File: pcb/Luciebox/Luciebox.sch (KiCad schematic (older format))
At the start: 60 parts, among them J1 Screw_Terminal_01x07, J2 Screw_Terminal_01x07, J3 Screw_Terminal_01x07, J4 Screw_Terminal_01x07, J5 Screw_Terminal_01x07, J7 USB_B_Mini, P1 CONN_01X01, P2 CONN_01X01, P3 CONN_01X01, P4 CONN_01X01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

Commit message: progressive change towards v2.0
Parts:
- removed J1: Screw_Terminal_01x07, Luciebox:Terminal_7x1_100mil, symbol Luciebox_components:Screw_Terminal_01x07_mirror
- added T? (x2): terminal_8x1, Luciebox:Terminal_8x1_100mil, symbol Luciebox_components:terminal_8x1
- R1, R10, R11, R12, R13, R14, R15, R16, R17, R18, R19, R2, R3, R4, R47, R48, R49, R5, R6, R7, R8, R9: footprint Luciebox:1206 -> Luciebox:1206_0805
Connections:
- net 0(Rx): now also T?.8
- net 12(MISO): now also T?.5
- net 13(SCK): now also T?.6
- net 2: now also T?.2
- net 3(PWM): now also T?.7
- net 4: now also T?.3
- net 7: now also T?.1
- net 8: now also T?.4
- net VCC: now also T?.1, T?.2, T?.3, T?.4, T?.5, T?.6, T?.7, T?.8
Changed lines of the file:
@@
 F 0 "R3" H 7059 2446 50  0000 L CNN
 F 1 "100" H 7059 2355 50  0000 L CNN
-F 2 "Luciebox:1206" H 7000 2400 50  0001 C CNN
+F 2 "Luciebox:1206_0805" H 7000 2400 50  0001 C CNN
 F 3 "~" H 7000 2400 50  0001 C CNN
 	1    7000 2400
@@
 F 0 "R4" H 7309 2446 50  0000 L CNN
 F 1 "100" H 7309 2355 50  0000 L CNN
-F 2 "Luciebox:1206" H 7250 2400 50  0001 C CNN
+F 2 "Luciebox:1206_0805" H 7250 2400 50  0001 C CNN
 F 3 "~" H 7250 2400 50  0001 C CNN
 	1    7250 2400
@@
 F 0 "R5" H 7559 2446 50  0000 L CNN
 F 1 "100" H 7559 2355 50  0000 L CNN
-F 2 "Luciebox:1206" H 7500 2400 50  0001 C CNN
+F 2 "Luciebox:1206_0805" H 7500 2400 50  0001 C CNN
 F 3 "~" H 7500 2400 50  0001 C CNN
 	1    7500 2400
@@
 	3350 1600 3500 1600
 Wire Wire Line
-	3350 1700 3850 1700
-Wire Wire Line
 	3700 2500 3700 1200
 Connection ~ 3700 1200
@@
 F 0 "R2" H 6809 2446 50  0000 L CNN
 F 1 "100" H 6809 2355 50  0000 L CNN
-F 2 "Luciebox:1206" H 6750 2400 50  0001 C CNN
+F 2 "Luciebox:1206_0805" H 6750 2400 50  0001 C CNN
 F 3 "~" H 6750 2400 50  0001 C CNN
 	1    6750 2400
@@
 F 0 "R1" H 6559 2446 50  0000 L CNN
 F 1 "100" H 6559 2355 50  0000 L CNN
-F 2 "Luciebox:1206" H 6500 2400 50  0001 C CNN
+F 2 "Luciebox:1206_0805" H 6500 2400 50  0001 C CNN
 F 3 "~" H 6500 2400 50  0001 C CNN
 	1    6500 2400
@@
 F 3 "~" H 5450 2600 50  0001 C CNN
 	1    5450 2600
-	1    0    0    -1
-$EndComp
-$Comp
-L Luciebox_components:Screw_Terminal_01x07_mirror J1
-U 1 1 5D554824
-P 3200 2600
-F 0 "J1" H 3282 3117 50  0000 C CNN
-F 1 "Screw_Terminal_01x07" H 3282 3026 50  0000 C CNN
-F 2 "Luciebox:Terminal_7x1_100mil" H 3200 2600 50  0001 C CNN
-F 3 "~" H 3200 2600 50  0001 C CNN
-	1    3200 2600
 	1    0    0    -1
 $EndComp
@@
 F 0 "R7" H 1009 4946 50  0000 L CNN
 F 1 "10K" H 1009 4855 50  0000 L CNN
-F 2 "Luciebox:1206" H 950 4900 50  0001 C CNN
+F 2 "Luciebox:1206_0805" H 950 4900 50  0001 C CNN
 F 3 "~" H 950 4900 50  0001 C CNN
 	1    950  4900
@@
 F 0 "R8" H 1309 4946 50  0000 L CNN
 F 1 "10K" H 1309 4855 50  0000 L CNN
-F 2 "Luciebox:1206" H 1250 4900 50  0001 C CNN
+F 2 "Luciebox:1206_0805" H 1250 4900 50  0001 C CNN
 F 3 "~" H 1250 4900 50  0001 C CNN
 	1    1250 4900
@@
 F 0 "R9" H 1609 4946 50  0000 L CNN
 F 1 "10K" H 1609 4855 50  0000 L CNN
-F 2 "Luciebox:1206" H 1550 4900 50  0001 C CNN
+F 2 "Luciebox:1206_0805" H 1550 4900 50  0001 C CNN
 F 3 "~" H 1550 4900 50  0001 C CNN
 	1    1550 4900
@@
 F 0 "R10" H 1909 4946 50  0000 L CNN
 F 1 "10K" H 1909 4855 50  0000 L CNN
-F 2 "Luciebox:1206" H 1850 4900 50  0001 C CNN
+F 2 "Luciebox:1206_0805" H 1850 4900 50  0001 C CNN
 F 3 "~" H 1850 4900 50  0001 C CNN
 	1    1850 4900
@@
 F 0 "R11" H 2209 4946 50  0000 L CNN
 F 1 "10K" H 2209 4855 50  0000 L CNN
-F 2 "Luciebox:1206" H 2150 4900 50  0001 C CNN
+F 2 "Luciebox:1206_0805" H 2150 4900 50  0001 C CNN
 F 3 "~" H 2150 4900 50  0001 C CNN
 	1    2150 4900
@@
 F 0 "R12" H 2509 4946 50  0000 L CNN
 F 1 "10K" H 2509 4855 50  0000 L CNN
-F 2 "Luciebox:1206" H 2450 4900 50  0001 C CNN
+F 2 "Luciebox:1206_0805" H 2450 4900 50  0001 C CNN
 F 3 "~" H 2450 4900 50  0001 C CNN
 	1    2450 4900
@@
 F 0 "R13" H 2809 4946 50  0000 L CNN
 F 1 "10K" H 2809 4855 50  0000 L CNN
-F 2 "Luciebox:1206" H 2750 4900 50  0001 C CNN
+F 2 "Luciebox:1206_0805" H 2750 4900 50  0001 C CNN
 F 3 "~" H 2750 4900 50  0001 C CNN
 	1    2750 4900
@@
 F 0 "R14" H 3109 4946 50  0000 L CNN
 F 1 "10K" H 3109 4855 50  0000 L CNN
-F 2 "Luciebox:1206" H 3050 4900 50  0001 C CNN
+F 2 "Luciebox:1206_0805" H 3050 4900 50  0001 C CNN
 F 3 "~" H 3050 4900 50  0001 C CNN
 	1    3050 4900
@@
 F 0 "R15" H 3409 4946 50  0000 L CNN
 F 1 "10K" H 3409 4855 50  0000 L CNN
-F 2 "Luciebox:1206" H 3350 4900 50  0001 C CNN
+F 2 "Luciebox:1206_0805" H 3350 4900 50  0001 C CNN
 F 3 "~" H 3350 4900 50  0001 C CNN
 	1    3350 4900
@@
 F 0 "R16" H 3709 4946 50  0000 L CNN
 F 1 "10K" H 3709 4855 50  0000 L CNN
-F 2 "Luciebox:1206" H 3650 4900 50  0001 C CNN
+F 2 "Luciebox:1206_0805" H 3650 4900 50  0001 C CNN
 F 3 "~" H 3650 4900 50  0001 C CNN
 	1    3650 4900
@@
 F 0 "R17" H 4009 4946 50  0000 L CNN
 F 1 "10K" H 4009 4855 50  0000 L CNN
-F 2 "Luciebox:1206" H 3950 4900 50  0001 C CNN
+F 2 "Luciebox:1206_0805" H 3950 4900 50  0001 C CNN
 F 3 "~" H 3950 4900 50  0001 C CNN
 	1    3950 4900
@@
 F 0 "R18" H 4309 4946 50  0000 L CNN
 F 1 "10K" H 4309 4855 50  0000 L CNN
-F 2 "Luciebox:1206" H 4250 4900 50  0001 C CNN
+F 2 "Luciebox:1206_0805" H 4250 4900 50  0001 C CNN
 F 3 "~" H 4250 4900 50  0001 C CNN
 	1    4250 4900
@@
 F 0 "R6" H 9359 4496 50  0000 L CNN
 F 1 "1M" H 9359 4405 50  0000 L CNN
-F 2 "Luciebox:1206" H 9300 4450 50  0001 C CNN
+F 2 "Luciebox:1206_0805" H 9300 4450 50  0001 C CNN
 F 3 "~" H 9300 4450 50  0001 C CNN
 	1    9300 4450
@@
 F 0 "R19" H 9559 5296 50  0000 L CNN
 F 1 "100" H 9559 5205 50  0000 L CNN
-F 2 "Luciebox:1206" H 9500 5250 50  0001 C CNN
+F 2 "Luciebox:1206_0805" H 9500 5250 50  0001 C CNN
 F 3 "~" H 9500 5250 50  0001 C CNN
 	1    9500 5250
@@
 F 0 "R47" H 3409 6646 50  0000 L CNN
 F 1 "100K" H 3409 6555 50  0000 L CNN
-F 2 "Luciebox:1206" H 3350 6600 50  0001 C CNN
+F 2 "Luciebox:1206_0805" H 3350 6600 50  0001 C CNN
 F 3 "~" H 3350 6600 50  0001 C CNN
 	1    3350 6600
@@
 F 0 "R48" H 3409 7046 50  0000 L CNN
 F 1 "100K" H 3409 6955 50  0000 L CNN
-F 2 "Luciebox:1206" H 3350 7000 50  0001 C CNN
+F 2 "Luciebox:1206_0805" H 3350 7000 50  0001 C CNN
 F 3 "~" H 3350 7000 50  0001 C CNN
 	1    3350 7000
@@
 F 0 "R49" H 3109 3546 50  0000 L CNN
 F 1 "10K" H 3109 3455 50  0000 L CNN
-F 2 "Luciebox:1206" H 3050 3500 50  0001 C CNN
+F 2 "Luciebox:1206_0805" H 3050 3500 50  0001 C CNN
 F 3 "~" H 3050 3500 50  0001 C CNN
 	1    3050 3500
@@
 Wire Wire Line
 	4150 5600 4050 5600
+$Comp
+L power:VCC #PWR?
+U 1 1 5E92F10F
+P 2250 2350
+F 0 "#PWR?" H 2250 2200 50  0001 C CNN
+F 1 "VCC" H 2267 2523 50  0000 C CNN
+F 2 "" H 2250 2350 50  0001 C CNN
+F 3 "" H 2250 2350 50  0001 C CNN
+	1    2250 2350
+	1    0    0    -1
+$EndComp
+$Comp
+L Luciebox_components:terminal_8x1 T?
+U 1 1 5E94AD11
+P 3350 2300
+F 0 "T?" H 3467 2085 50  0000 C CNN
+F 1 "terminal_8x1" H 3467 2176 50  0000 C CNN
+F 2 "Luciebox:Terminal_8x1_100mil" H 3150 2200 50  0001 C CNN
+F 3 "" H 3300 3400 50  0001 C CNN
+	1    3350 2300
+	-1   0    0    1
+$EndComp
+$Comp
+L Luciebox_components:terminal_8x1 T?
+U 1 1 5E968FAE
+P 2600 2300
+F 0 "T?" H 2717 2085 50  0000 C CNN
+F 1 "terminal_8x1" H 2717 2176 50  0000 C CNN
+F 2 "Luciebox:Terminal_8x1_100mil" H 2400 2200 50  0001 C CNN
+F 3 "" H 2550 3400 50  0001 C CNN
+	1    2600 2300
+	1    0    0    1
+$EndComp
+Wire Wire Line
+	2550 2300 2300 2300
+Wire Wire Line
+	2300 2300 2300 2350
+Wire Wire Line
+	2300 2350 2250 2350
+Wire Wire Line
+	2550 2400 2300 2400
+Wire Wire Line
+	2300 2400 2300 2350
+Connection ~ 2300 2350
+Wire Wire Line
+	2550 2500 2300 2500
+Wire Wire Line
+	2300 2500 2300 2400
+Connection ~ 2300 2400
+Wire Wire Line
+	2300 2500 2300 2600
+Wire Wire Line
+	2300 2600 2550 2600
+Connection ~ 2300 2500
+Wire Wire Line
+	2550 2700 2300 2700
+Wire Wire Line
+	2300 2700 2300 2600
+Connection ~ 2300 2600
+Wire Wire Line
+	2550 2800 2300 2800
+Wire Wire Line
+	2300 2800 2300 2700
+Connection ~ 2300 2700
+Wire Wire Line
+	2550 2900 2300 2900
+Wire Wire Line
+	2300 2900 2300 2800
+Connection ~ 2300 2800
+Wire Wire Line
+	2550 3000 2300 3000
+Wire Wire Line
+	2300 3000 2300 2900
+Connection ~ 2300 2900
+Wire Wire Line
+	3350 1700 3450 1700
+Wire Wire Line
+	3400 3000 3450 3000
+Wire Wire Line
+	3450 3000 3450 1700
+Connection ~ 3450 1700
+Wire Wire Line
+	3450 1700 3850 1700
 $EndSCHEMATC

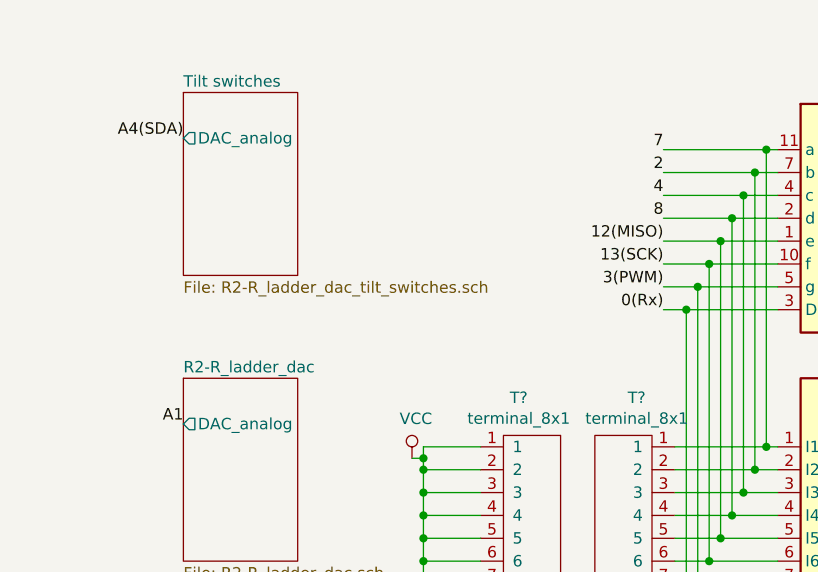
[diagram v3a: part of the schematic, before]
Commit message: add holes for R-2R ladder, fix bug with tilt switch sheet. Set output led's. All good here.
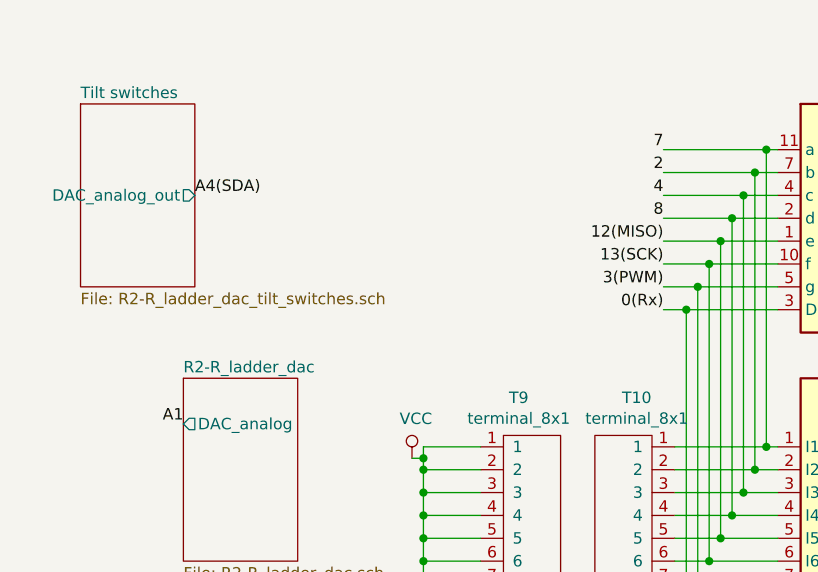
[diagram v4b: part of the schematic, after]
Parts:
- gave numbers to parts that had none: 2
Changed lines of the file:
@@
 Text Label 7000 2500 3    50   ~ 0
 9(PWM)
-Text Label 3350 1000 2    50   ~ 0
-7
 Wire Wire Line
 	3850 1000 3800 1000
 Wire Wire Line
 	3850 1100 3750 1100
-Text Label 3350 1100 2    50   ~ 0
-2
-Text Label 3350 1200 2    50   ~ 0
-4
-Text Label 3350 1300 2    50   ~ 0
-8
 Text Label 3350 1400 2    50   ~ 0
 12(MISO)
@@
 Text Label 1250 6250 2    50   ~ 0
 A3
-$Sheet
-S 1250 750  500  800
-U 5D9307E8
-F0 "Tilt switches" 50
-F1 "R2-R_ladder_dac_tilt_switches.sch" 50
-F2 "DAC_analog" O L 1250 950 50
-$EndSheet
-Text Label 1250 950  2    50   ~ 0
-A4(SDA)
 $Comp
 L Device:Buzzer BZ1
@@
 	4150 5600 4050 5600
 $Comp
-L power:VCC #PWR?
+L power:VCC #PWR0107
 U 1 1 5E92F10F
 P 2250 2350
-F 0 "#PWR?" H 2250 2200 50  0001 C CNN
+F 0 "#PWR0107" H 2250 2200 50  0001 C CNN
 F 1 "VCC" H 2267 2523 50  0000 C CNN
 F 2 "" H 2250 2350 50  0001 C CNN
@@
 $EndComp
 $Comp
-L Luciebox_components:terminal_8x1 T?
+L Luciebox_components:terminal_8x1 T10
 U 1 1 5E94AD11
 P 3350 2300
-F 0 "T?" H 3467 2085 50  0000 C CNN
+F 0 "T10" H 3467 2085 50  0000 C CNN
 F 1 "terminal_8x1" H 3467 2176 50  0000 C CNN
 F 2 "Luciebox:Terminal_8x1_100mil" H 3150 2200 50  0001 C CNN
@@
 $EndComp
 $Comp
-L Luciebox_components:terminal_8x1 T?
+L Luciebox_components:terminal_8x1 T9
 U 1 1 5E968FAE
 P 2600 2300
-F 0 "T?" H 2717 2085 50  0000 C CNN
+F 0 "T9" H 2717 2085 50  0000 C CNN
 F 1 "terminal_8x1" H 2717 2176 50  0000 C CNN
 F 2 "Luciebox:Terminal_8x1_100mil" H 2400 2200 50  0001 C CNN
@@
 Wire Wire Line
 	3450 1700 3850 1700
+Text Label 1300 1200 0    50   ~ 0
+A4(SDA)
+Text Label 3350 1300 2    50   ~ 0
+8
+Text Label 3350 1200 2    50   ~ 0
+4
+Text Label 3350 1100 2    50   ~ 0
+2
+Text Label 3350 1000 2    50   ~ 0
+7
+$Sheet
+S 800  800  500  800
+U 5D9307E8
+F0 "Tilt switches" 50
+F1 "R2-R_ladder_dac_tilt_switches.sch" 50
+F2 "DAC_analog_out" O R 1300 1200 50
+$EndSheet
 $EndSCHEMATC

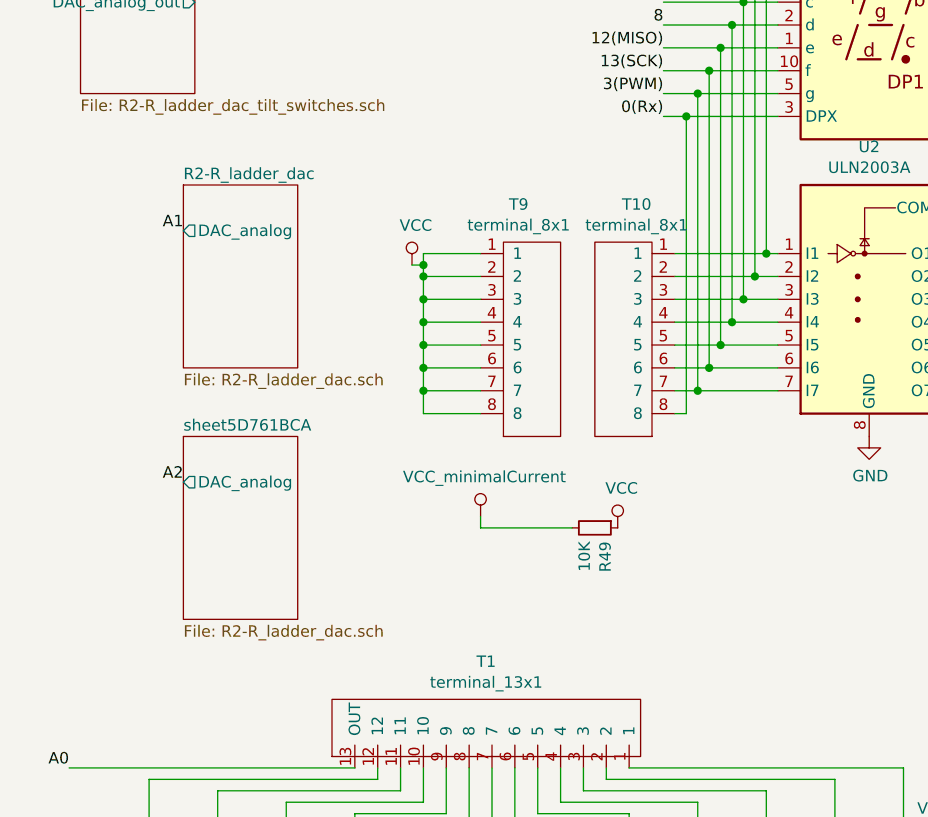
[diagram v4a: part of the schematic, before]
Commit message: modify pcb v2.0.  nearly finished. Choose box.
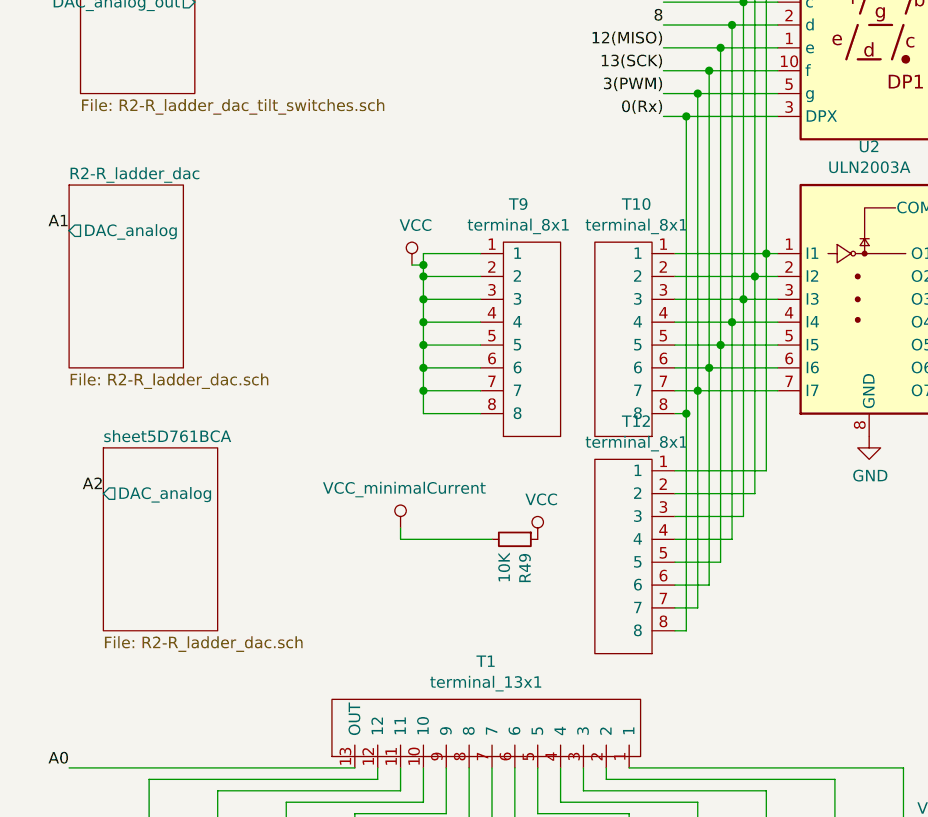
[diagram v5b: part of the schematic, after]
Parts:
- added T12: terminal_8x1, Luciebox:Terminal_8x1_100mil, symbol Luciebox_components:terminal_8x1
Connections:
- net 0(Rx): now also T12.8
- net 12(MISO): now also T12.5
- net 13(SCK): now also T12.6
- net 2: now also T12.2
- net 3(PWM): now also T12.7
- net 4: now also T12.3
- net 7: now also T12.1
- net 8: now also T12.4
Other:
- moved on the sheet: R49
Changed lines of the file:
@@
 $EndComp
 $Sheet
-S 1250 2000 500  800
+S 750  2000 500  800
 U 5D74964C
 F0 "R2-R_ladder_dac" 50
 F1 "R2-R_ladder_dac.sch" 50
-F2 "DAC_analog" O L 1250 2200 50
+F2 "DAC_analog" O L 750 2200 50
 $EndSheet
 $Sheet
-S 1250 3100 500  800
+S 900  3150 500  800
 U 5D761BCA
 F0 "sheet5D761BCA" 50
 F1 "R2-R_ladder_dac.sch" 50
-F2 "DAC_analog" O L 1250 3300 50
+F2 "DAC_analog" O L 900 3350 50
 $EndSheet
-Text Label 1250 2200 2    50   ~ 0
+Text Label 750  2200 2    50   ~ 0
 A1
-Text Label 1250 3300 2    50   ~ 0
+Text Label 900  3350 2    50   ~ 0
 A2
 $Comp
@@
 L Device:R_Small R49
 U 1 1 5E1772EF
-P 3050 3500
-F 0 "R49" H 3109 3546 50  0000 L CNN
-F 1 "10K" H 3109 3455 50  0000 L CNN
-F 2 "Luciebox:1206_0805" H 3050 3500 50  0001 C CNN
-F 3 "~" H 3050 3500 50  0001 C CNN
-	1    3050 3500
+P 2700 3550
+F 0 "R49" H 2759 3596 50  0000 L CNN
+F 1 "10K" H 2759 3505 50  0000 L CNN
+F 2 "Luciebox:1206_0805" H 2700 3550 50  0001 C CNN
+F 3 "~" H 2700 3550 50  0001 C CNN
+	1    2700 3550
 	0    1    1    0
 $EndComp
@@
 L power:VCC #PWR029
 U 1 1 5E19FB8B
-P 3150 3500
-F 0 "#PWR029" H 3150 3350 50  0001 C CNN
-F 1 "VCC" H 3167 3673 50  0000 C CNN
-F 2 "" H 3150 3500 50  0001 C CNN
-F 3 "" H 3150 3500 50  0001 C CNN
-	1    3150 3500
+P 2800 3550
+F 0 "#PWR029" H 2800 3400 50  0001 C CNN
+F 1 "VCC" H 2817 3723 50  0000 C CNN
+F 2 "" H 2800 3550 50  0001 C CNN
+F 3 "" H 2800 3550 50  0001 C CNN
+	1    2800 3550
 	1    0    0    -1
 $EndComp
@@
 L Luciebox_components:VCC_minimalCurrent #PWR028
 U 1 1 5E1A5201
-P 2550 3450
-F 0 "#PWR028" H 2550 3300 50  0001 C CNN
-F 1 "VCC_minimalCurrent" H 2567 3623 50  0000 C CNN
-F 2 "" H 2550 3450 50  0001 C CNN
-F 3 "" H 2550 3450 50  0001 C CNN
-	1    2550 3450
-	1    0    0    -1
-$EndComp
-Wire Wire Line
-	2950 3500 2550 3500
-Wire Wire Line
-	2550 3500 2550 3450
+P 2200 3500
+F 0 "#PWR028" H 2200 3350 50  0001 C CNN
+F 1 "VCC_minimalCurrent" H 2217 3673 50  0000 C CNN
+F 2 "" H 2200 3500 50  0001 C CNN
+F 3 "" H 2200 3500 50  0001 C CNN
+	1    2200 3500
+	1    0    0    -1
+$EndComp
+Wire Wire Line
+	2600 3550 2200 3550
+Wire Wire Line
+	2200 3550 2200 3500
 Wire Wire Line
 	1750 5850 2250 5850
@@
 F2 "DAC_analog_out" O R 1300 1200 50
 $EndSheet
+$Comp
+L Luciebox_components:terminal_8x1 T12
+U 1 1 5EE64EB9
+P 3350 3250
+F 0 "T12" H 3467 3035 50  0000 C CNN
+F 1 "terminal_8x1" H 3467 3126 50  0000 C CNN
+F 2 "Luciebox:Terminal_8x1_100mil" H 3150 3150 50  0001 C CNN
+F 3 "" H 3300 4350 50  0001 C CNN
+	1    3350 3250
+	-1   0    0    1
+$EndComp
+Wire Wire Line
+	3450 3000 3450 3950
+Wire Wire Line
+	3450 3950 3400 3950
+Connection ~ 3450 3000
+Wire Wire Line
+	3400 3850 3500 3850
+Wire Wire Line
+	3500 3850 3500 2900
+Wire Wire Line
+	3550 2800 3550 3750
+Wire Wire Line
+	3550 3750 3400 3750
+Wire Wire Line
+	3400 3650 3600 3650
+Wire Wire Line
+	3600 3650 3600 2700
+Wire Wire Line
+	3650 2600 3650 3550
+Wire Wire Line
+	3650 3550 3400 3550
+Wire Wire Line
+	3700 2500 3700 3450
+Wire Wire Line
+	3700 3450 3400 3450
+Wire Wire Line
+	3750 2400 3750 3350
+Wire Wire Line
+	3750 3350 3400 3350
+Wire Wire Line
+	3800 2300 3800 3250
+Wire Wire Line
+	3800 3250 3400 3250
 $EndSCHEMATC

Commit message: pcb change extra header so holes line up for lights to buttons.
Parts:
- removed T12: terminal_8x1, Luciebox:Terminal_8x1_100mil, symbol Luciebox_components:terminal_8x1
- added T13: terminal_8x1, Luciebox:Terminal_8x1_100mil, symbol Luciebox_components:terminal_8x1
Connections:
- net 0(Rx): now also T13.1
- net 12(MISO): now also T13.3
- net 13(SCK): now also T13.4
- net 2: now also T13.6
- net 3(PWM): now also T13.7
- net 4: now also T13.8
- net 7: now also T13.5
- net 8: now also T13.2
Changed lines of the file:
@@
 F2 "DAC_analog_out" O R 1300 1200 50
 $EndSheet
+Connection ~ 3450 3000
+Wire Wire Line
+	3700 2500 3700 3300
 $Comp
-L Luciebox_components:terminal_8x1 T12
-U 1 1 5EE64EB9
-P 3350 3250
-F 0 "T12" H 3467 3035 50  0000 C CNN
-F 1 "terminal_8x1" H 3467 3126 50  0000 C CNN
-F 2 "Luciebox:Terminal_8x1_100mil" H 3150 3150 50  0001 C CNN
-F 3 "" H 3300 4350 50  0001 C CNN
-	1    3350 3250
-	-1   0    0    1
+L Luciebox_components:terminal_8x1 T13
+U 1 1 5E835E31
+P 4000 4000
+F 0 "T13" H 4117 3785 50  0000 C CNN
+F 1 "terminal_8x1" H 4117 3876 50  0000 C CNN
+F 2 "Luciebox:Terminal_8x1_100mil" H 3800 3900 50  0001 C CNN
+F 3 "" H 3950 5100 50  0001 C CNN
+	1    4000 4000
+	1    0    0    -1
 $EndComp
 Wire Wire Line
-	3450 3000 3450 3950
+	3950 3300 3700 3300
 Wire Wire Line
-	3450 3950 3400 3950
-Connection ~ 3450 3000
+	3950 3400 3500 3400
 Wire Wire Line
-	3400 3850 3500 3850
+	3500 3400 3500 2900
 Wire Wire Line
-	3500 3850 3500 2900
+	3950 3500 3750 3500
 Wire Wire Line
-	3550 2800 3550 3750
+	3550 2800 3550 3700
 Wire Wire Line
-	3550 3750 3400 3750
+	3950 3700 3550 3700
 Wire Wire Line
-	3400 3650 3600 3650
+	3950 3800 3600 3800
 Wire Wire Line
-	3600 3650 3600 2700
+	3950 3900 3650 3900
 Wire Wire Line
-	3650 2600 3650 3550
+	3950 4000 3450 4000
 Wire Wire Line
-	3650 3550 3400 3550
+	3950 3600 3800 3600
 Wire Wire Line
-	3700 2500 3700 3450
+	3800 2300 3800 3600
 Wire Wire Line
-	3700 3450 3400 3450
+	3750 2400 3750 3500
 Wire Wire Line
-	3750 2400 3750 3350
+	3650 2600 3650 3900
 Wire Wire Line
-	3750 3350 3400 3350
+	3600 2700 3600 3800
 Wire Wire Line
-	3800 2300 3800 3250
-Wire Wire Line
-	3800 3250 3400 3250
+	3450 3000 3450 4000
 $EndSCHEMATC
